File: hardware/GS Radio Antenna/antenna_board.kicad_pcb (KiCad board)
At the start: 2 copper layers, 88.9 x 92.5 mm, 28 parts, among them J1 Conn_01x02_Socket, U10 IRF4905PBF, U11 IRF4905PBF, U12 IRF4905PBF, U2 ESP32-DEVKITC, U3 LM3940IT-3.3/NOPB, U4 TLC5916IN, U5 TLC5916IN, U6 TLC5916IN, U9 IRF4905PBF

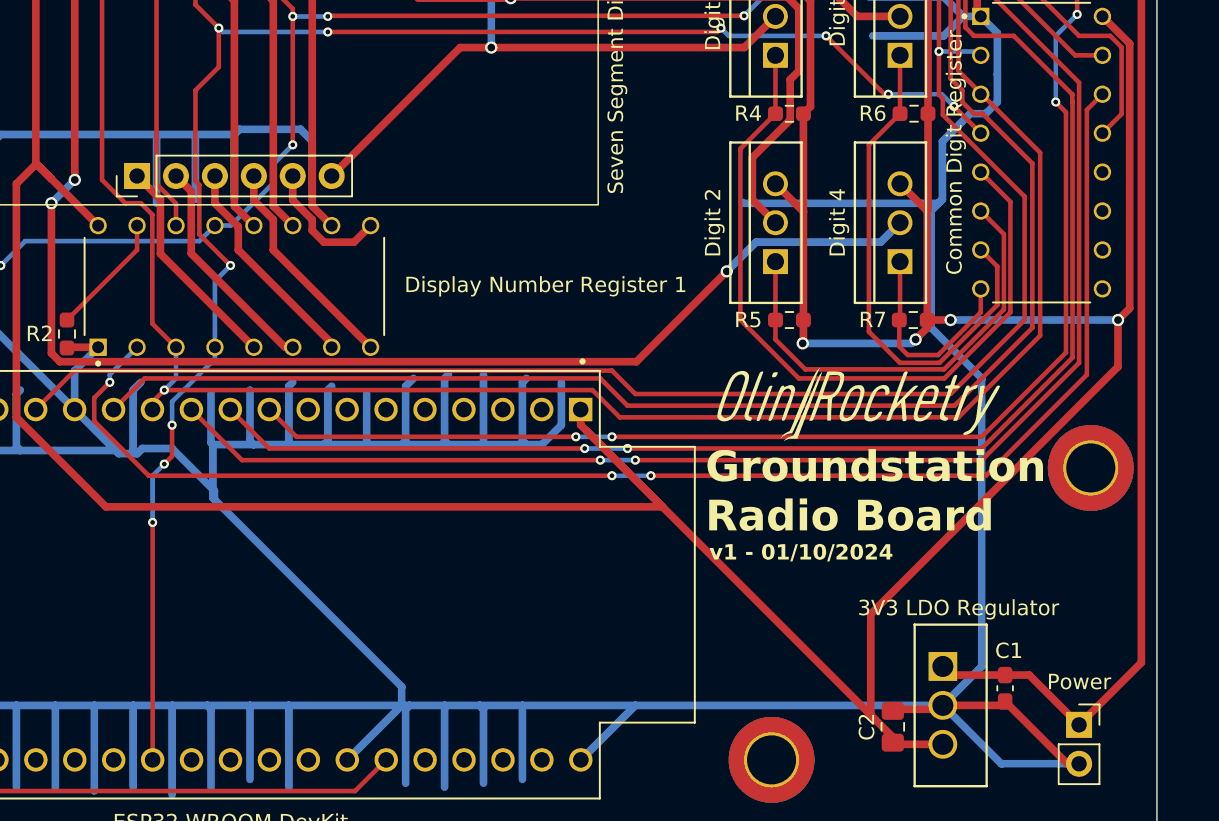
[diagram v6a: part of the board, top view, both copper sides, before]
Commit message: Add voltage divider to measure battery voltage
Added a voltage divider and connected it to one of the analog input pins of the ESP32 so we can actually measure the battery voltage
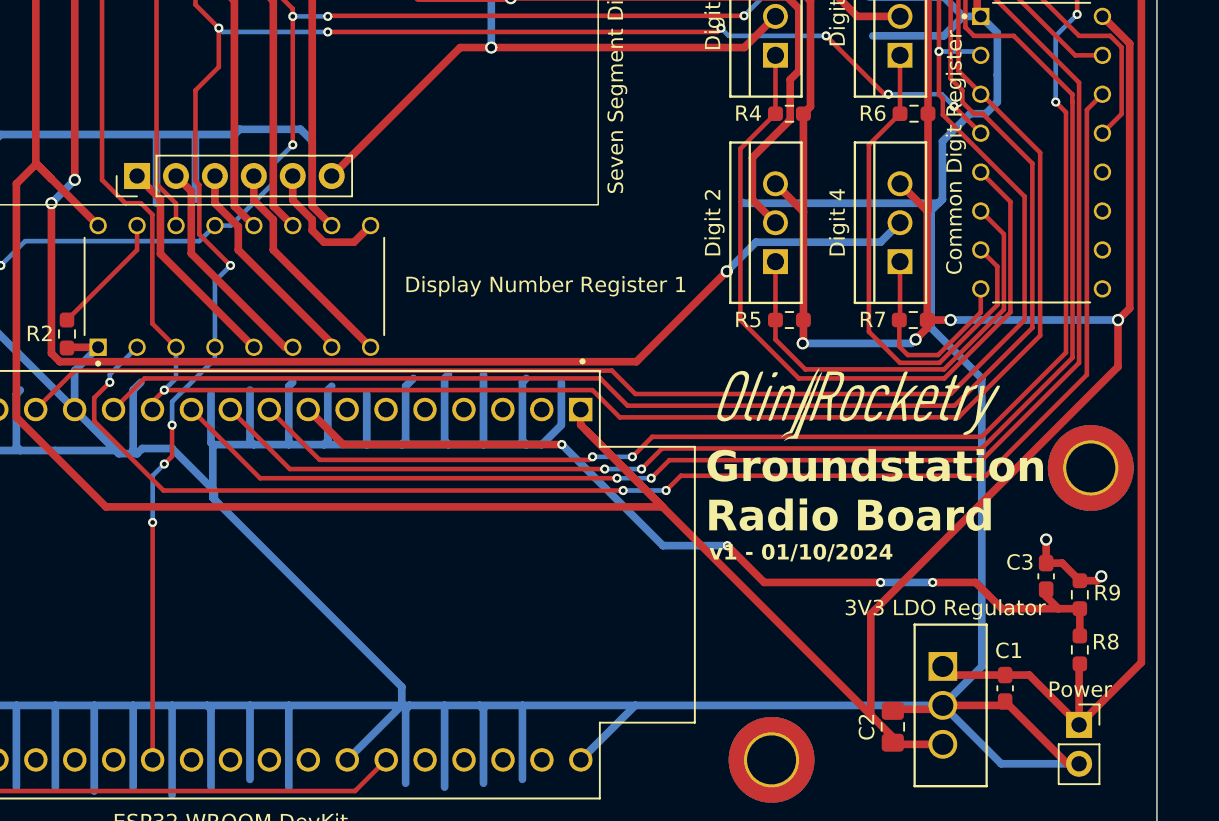
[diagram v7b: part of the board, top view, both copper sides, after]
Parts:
- added C3: 10uF, Capacitor_SMD:C_0603_1608Metric_Pad1.08x0.95mm_HandSolder, F.Cu at (182.0, 116.8)
- added R8: 10k, Resistor_SMD:R_0603_1608Metric_Pad0.98x0.95mm_HandSolder, F.Cu at (184.2, 121.6)
- added R9: 33k, Resistor_SMD:R_0603_1608Metric_Pad0.98x0.95mm_HandSolder, F.Cu at (184.2, 118.0)
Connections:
- U2 pad 8: unconnected-(U2-IO33-Pad8) -> Vout
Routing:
- net Vout: track 0.00 -> 59.3 mm, vias 0 -> 4
- net GND: track 726.4 -> 732.2 mm, vias 0 -> 2
- net VDD: track 93.7 -> 97.5 mm
- net /G0: track 103.9 -> 105.1 mm
- net /CS: track 96.9 -> 98.1 mm
- net /RST: track 99.1 -> 100.1 mm
- net Net-(U4-SDO): track 93.7 -> 94.5 mm

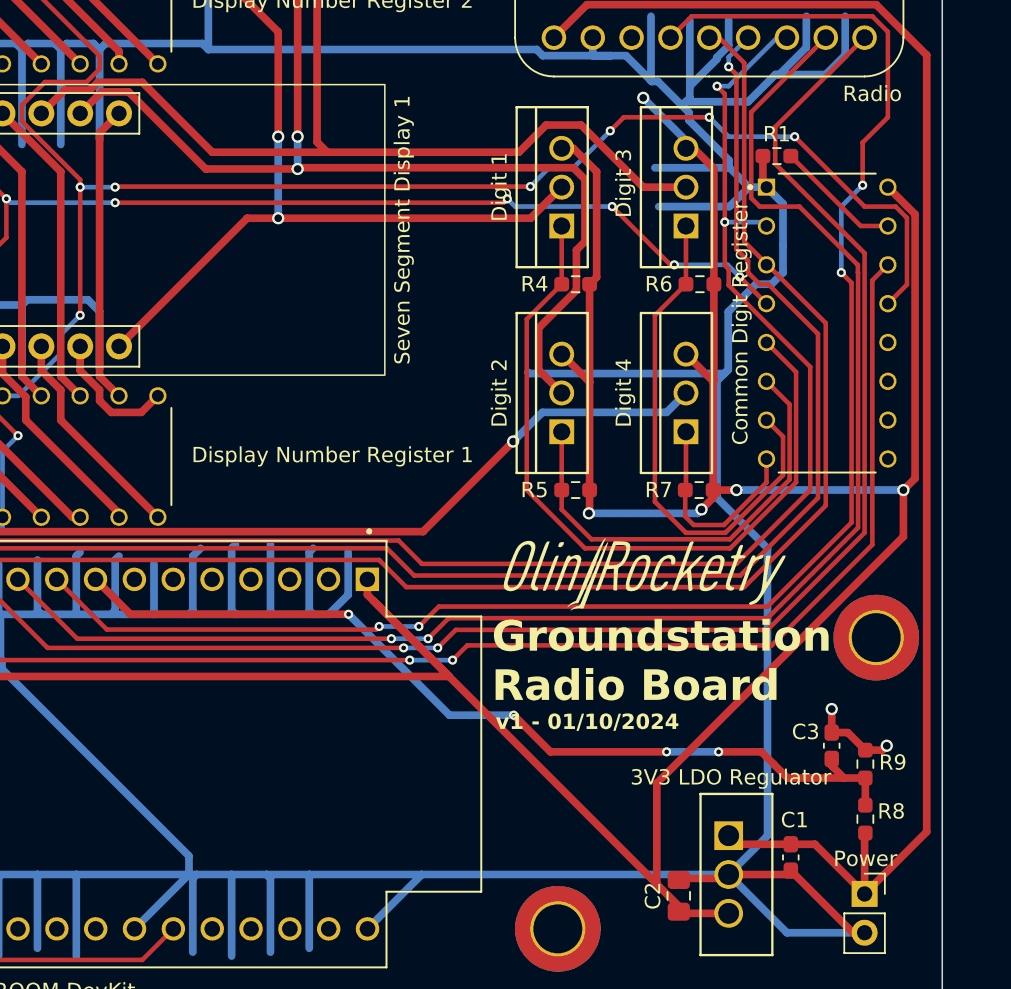
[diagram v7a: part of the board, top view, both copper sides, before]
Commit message: Move capacitor closer on Radio Board
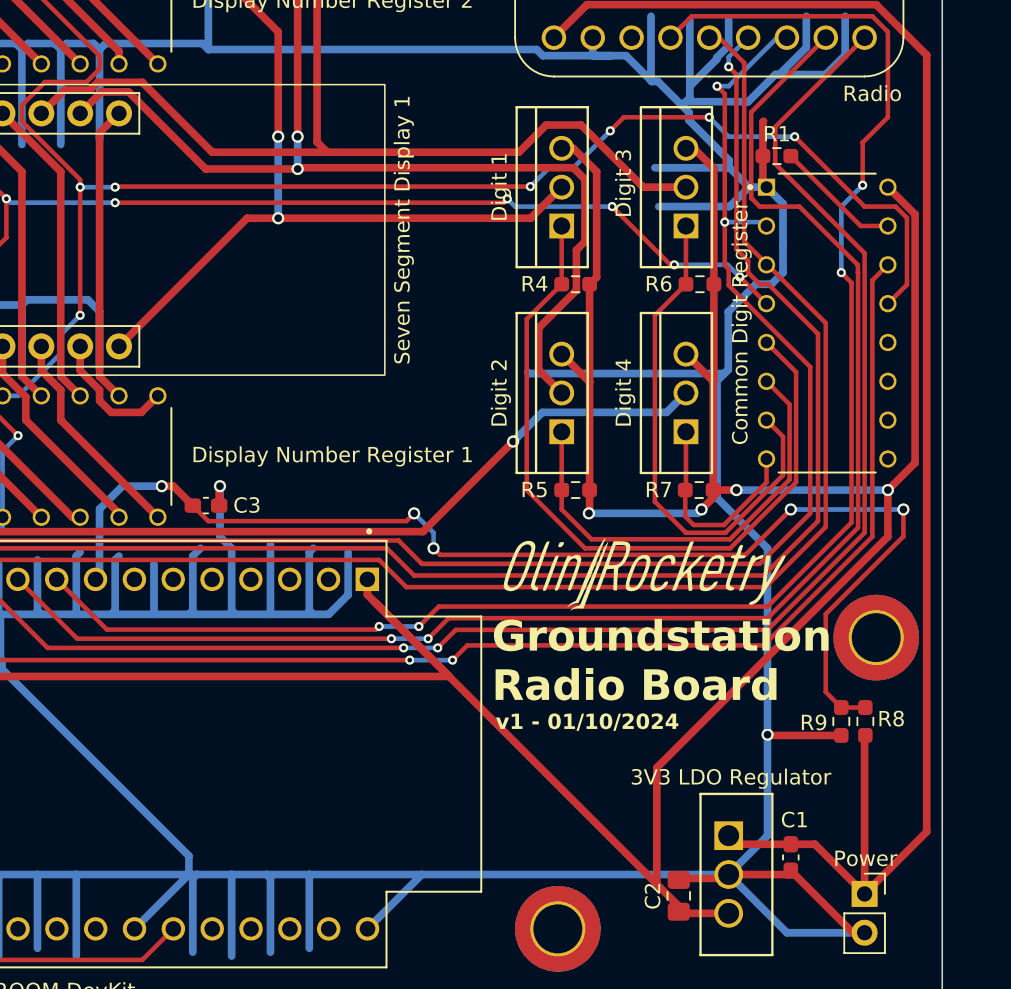
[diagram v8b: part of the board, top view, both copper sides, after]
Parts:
- moved C3 43.8 mm to (141.1, 101.1), turned to 0 degrees
- moved R8 6.39 mm to (184.2, 115.2)
- moved R9 3.20 mm to (182.6, 115.2), turned to -90 degrees
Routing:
- net Vout: track 59.3 -> 79.1 mm, vias 4 -> 5
- net GND: track 732.2 -> 738.9 mm
- net VDD: track 97.5 -> 104.0 mm
- net /3.3V: track 269.7 -> 264.7 mm, vias 5 -> 4
- net /MOSI: track 105.9 -> 106.8 mm
- net /MISO: track 97.0 -> 97.9 mm
- net /SCK: track 134.2 -> 135.0 mm
- added copper zone on F.Cu, net GND
- removed copper zone on F.Cu, net /3.3V
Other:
- board text added: "Jojo Liu"
- board text added: "Lili Baker"
- board text added: "Rishit Bansal"
- board text removed: "Joseph Liu"
